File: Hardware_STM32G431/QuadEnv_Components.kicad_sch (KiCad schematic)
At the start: 54 parts, among them J1 Conn_01x04_Male, J2 Conn_01x04_Male, J3 Conn_01x04_Male, J4 Conn_01x04_Male, J5 SWD_Header, J6 Eurorack_10_pin_power, J7 USB_B_Micro, U1 STM32G431C6T6, U2 LD1117-3.3-4Tab, U3 CD40109B, U4 TL074

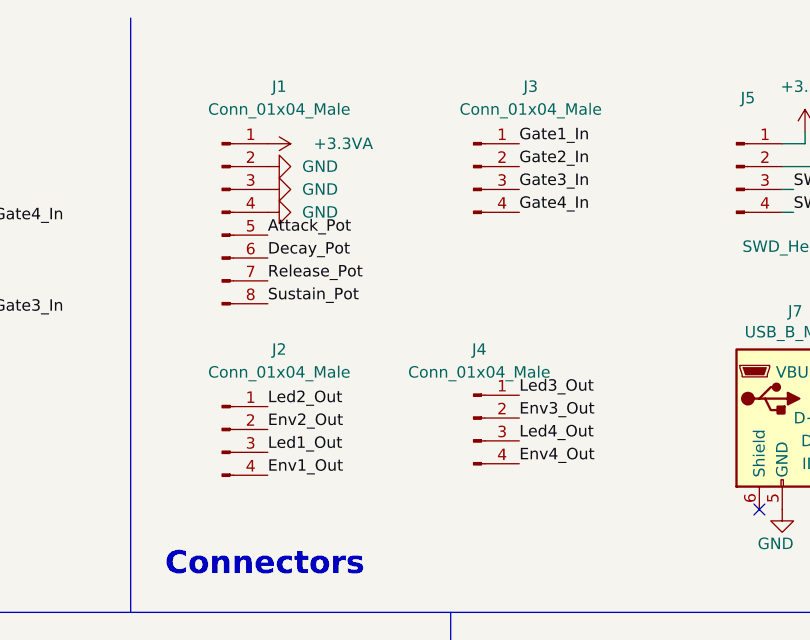
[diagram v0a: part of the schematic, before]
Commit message: First draft of control PCB complete
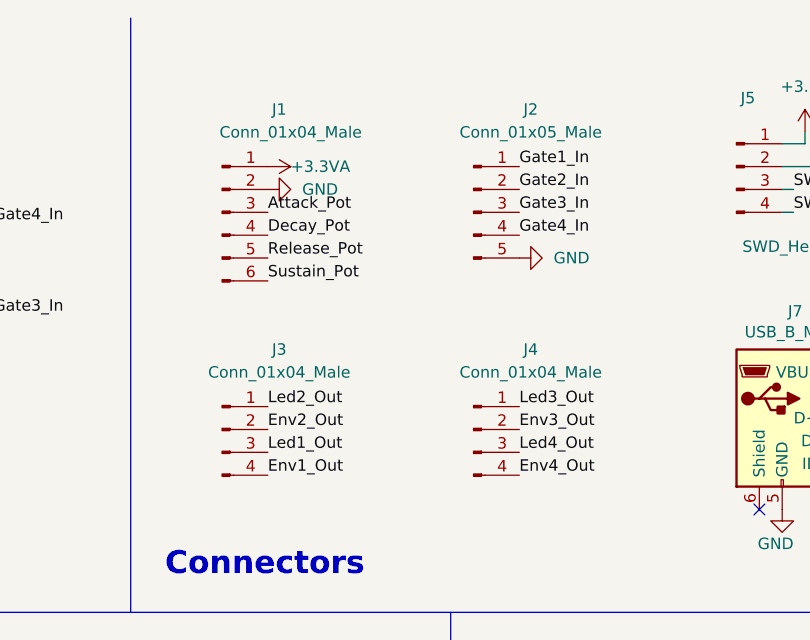
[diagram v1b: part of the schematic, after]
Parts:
- J1: footprint Connector_PinHeader_2.54mm:PinHeader_1x08_P2.54mm_Vertical -> Connector_PinSocket_2.54mm:PinSocket_1x06_P2.54mm_Vertical; symbol Connector:Conn_01x08_Male -> Connector:Conn_01x06_Male
- J2: renamed from J3; value Conn_01x04_Male -> Conn_01x05_Male; footprint Connector_PinHeader_2.54mm:PinHeader_1x04_P2.54mm_Vertical -> Connector_PinSocket_2.54mm:PinSocket_1x05_P2.54mm_Vertical; symbol Connector:Conn_01x04_Male -> Connector:Conn_01x05_Male
- J3: renamed from J2; footprint Connector_PinHeader_2.54mm:PinHeader_1x04_P2.54mm_Vertical -> Connector_PinSocket_2.54mm:PinSocket_1x04_P2.54mm_Vertical
- J4: footprint Connector_PinHeader_2.54mm:PinHeader_1x04_P2.54mm_Vertical -> Connector_PinSocket_2.54mm:PinSocket_1x04_P2.54mm_Vertical
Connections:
- net Attack_Pot: now also J1.3 (Pin_3); no longer J1.5 (Pin_5)
- net Decay_Pot: now also J1.4 (Pin_4); no longer J1.6 (Pin_6)
- net GND: now also J2.5 (Pin_5); no longer J1.3 (Pin_3), J1.4 (Pin_4)
- net Release_Pot: now also J1.5 (Pin_5); no longer J1.7 (Pin_7)
- net Sustain_Pot: now also J1.6 (Pin_6); no longer J1.8 (Pin_8)
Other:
- moved on the sheet: J4

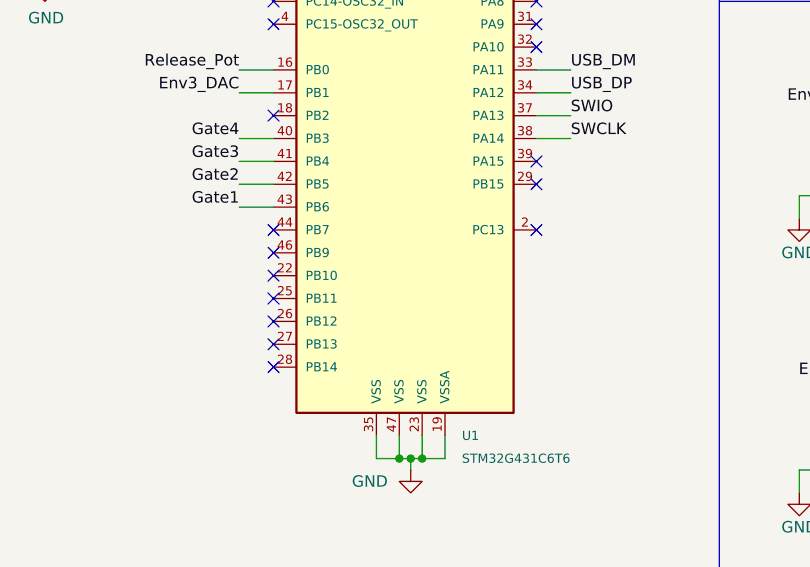
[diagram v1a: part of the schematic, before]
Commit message: Added PWM Test code
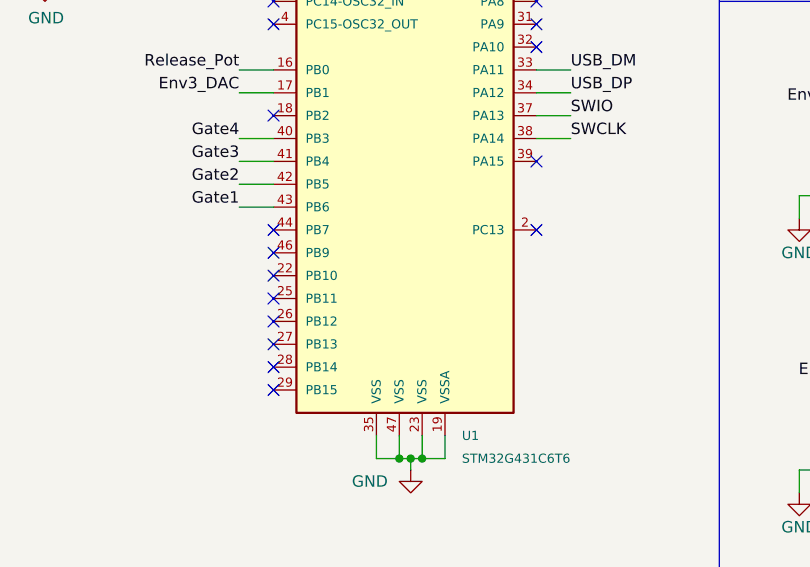
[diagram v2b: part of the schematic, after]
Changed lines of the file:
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@@
   (no_connect (at 45.72 78.74))
   (no_connect (at 261.62 67.31))
-  (no_connect (at 74.93 99.06))
+  (no_connect (at 45.72 121.92))
   (wire (pts (xy 198.12 118.11) (xy 198.12 123.19))
     (stroke (width 0) (type solid) (color 0 0 0 0))

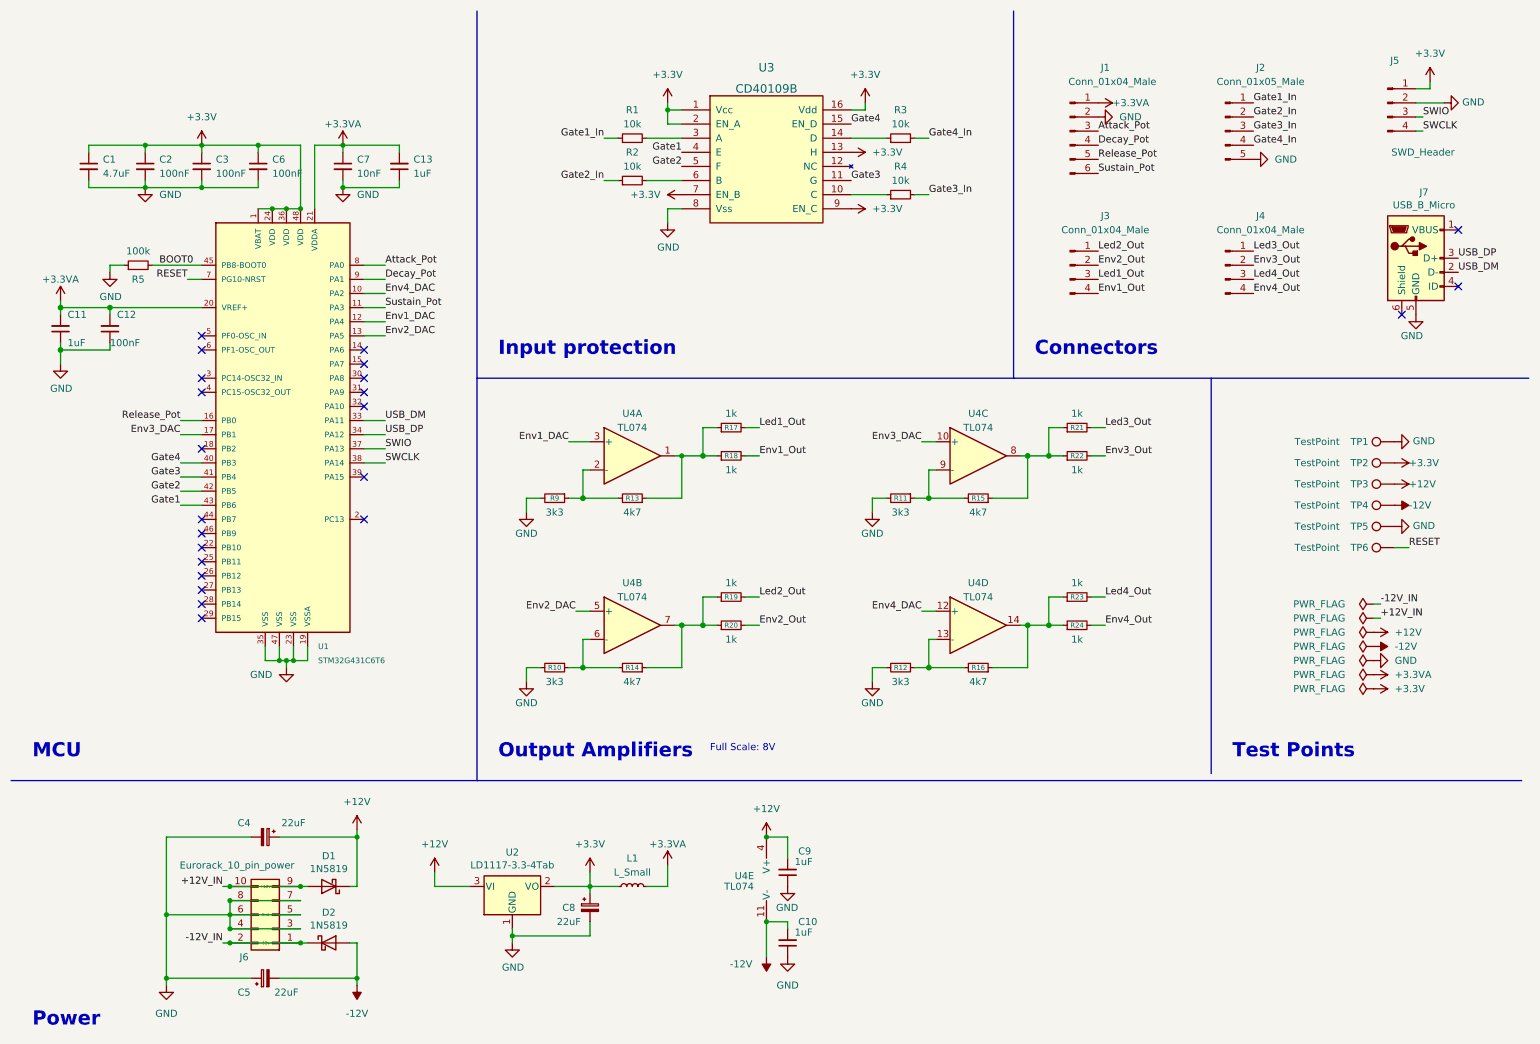
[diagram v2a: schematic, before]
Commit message: Clean up project for manufacture
Fixed LED ordering bug on control board
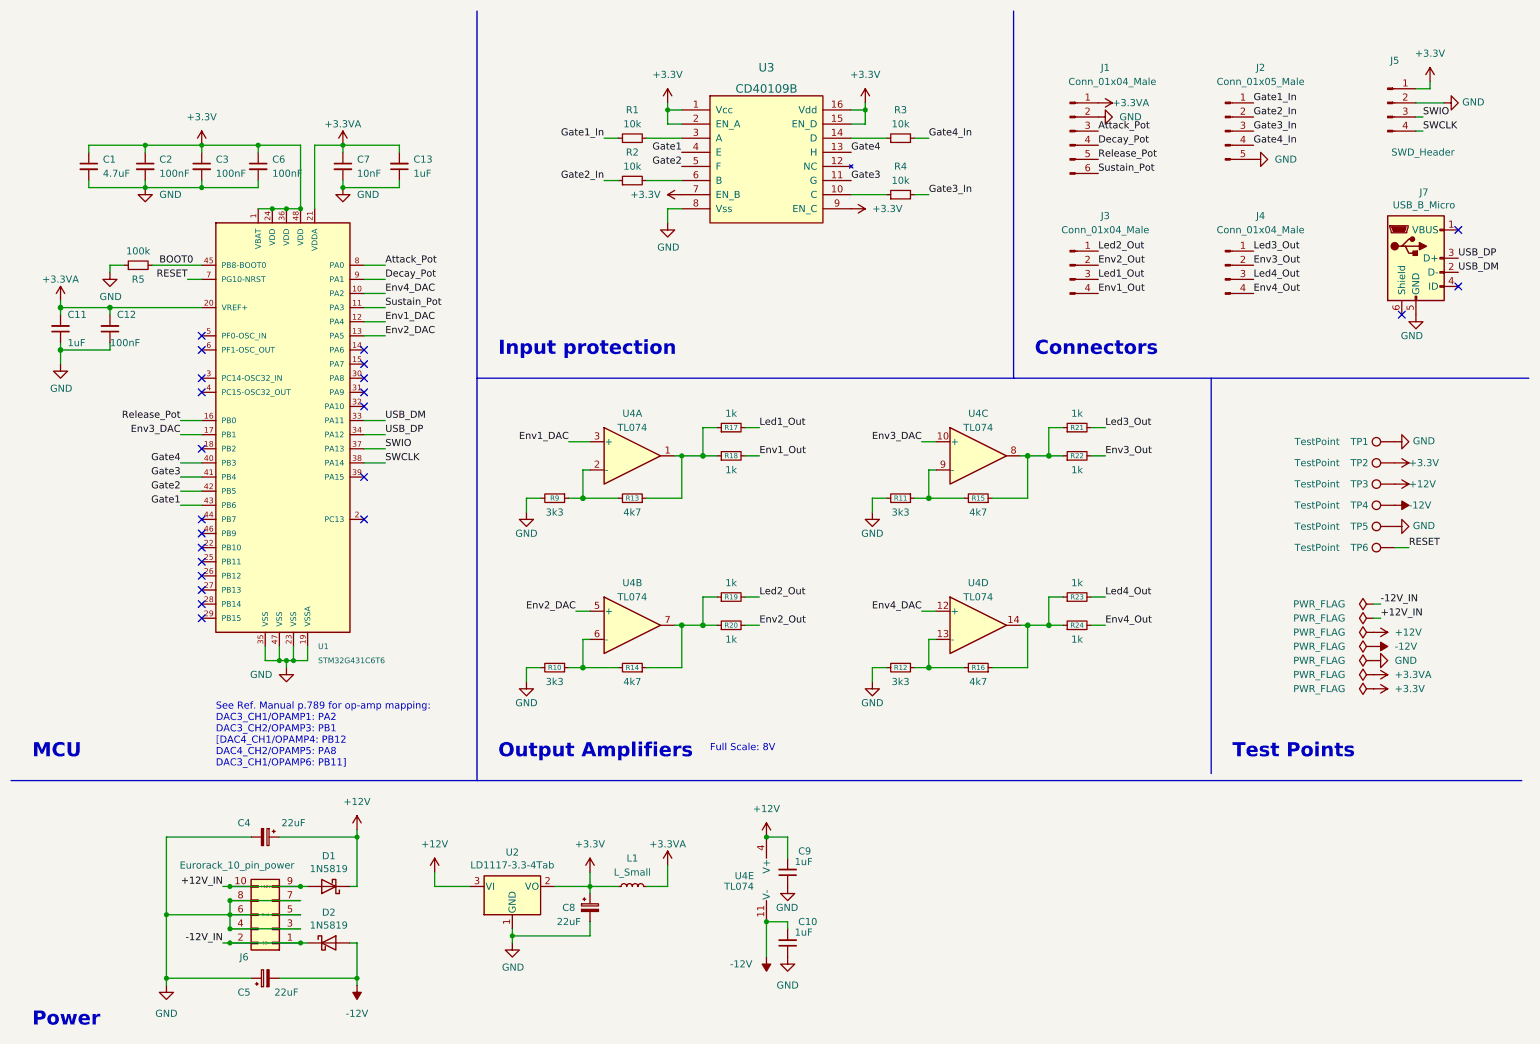
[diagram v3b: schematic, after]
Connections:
- net +3.3V: now also U3.15 (EN_D); no longer U3.13 (H)
- net Gate4: now also U3.13 (H); no longer U3.15 (EN_D)
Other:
- note added: "See Ref. Manual p.789 for op-amp mapping: DAC3_CH1/OPAMP1: PA2 DAC3_CH2/OPAMP3: PB1 [DAC4_CH1/OPAMP4: PB12 DAC4_CH2/OPAMP5: PA8 DAC3_CH1/OPAMP6: PB11]"
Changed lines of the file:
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@@
   (junction (at 73.66 186.69) (diameter 0) (color 0 0 0 0)
+  )
+  (junction (at 165.1 30.48) (diameter 0) (color 0 0 0 0)
   )
   (junction (at 147.32 176.53) (diameter 0) (color 0 0 0 0)
@@
     (stroke (width 0) (type default) (color 0 0 0 0))
   )
+  (wire (pts (xy 162.56 33.02) (xy 165.1 33.02))
+    (stroke (width 0) (type default) (color 0 0 0 0))
+  )
   (wire (pts (xy 101.6 177.8) (xy 101.6 179.07))
     (stroke (width 0) (type default) (color 0 0 0 0))
@@
     (stroke (width 0) (type default) (color 0 0 0 0))
   )
+  (wire (pts (xy 165.1 33.02) (xy 165.1 30.48))
+    (stroke (width 0) (type default) (color 0 0 0 0))
+  )
   (wire (pts (xy 151.13 176.53) (xy 151.13 177.8))
     (stroke (width 0) (type default) (color 0 0 0 0))
@@
   (wire (pts (xy 115.57 167.64) (xy 115.57 170.18))
     (stroke (width 0) (type default) (color 0 0 0 0))
+  )
+  (text "See Ref. Manual p.789 for op-amp mapping:\nDAC3_CH1/OPAMP1: PA2\nDAC3_CH2/OPAMP3: PB1\n[DAC4_CH1/OPAMP4: PB12\nDAC4_CH2/OPAMP5: PA8\nDAC3_CH1/OPAMP6: PB11]\n\n\n\n"
+    (at 48.26 154.94 0)
+    (effects (font (size 1.27 1.27)) (justify left bottom))
   )
   (text "Full Scale: 8V" (at 137.16 146.05 0)
@@
     (effects (font (size 1.27 1.27)) (justify left bottom))
   )
-  (label "Gate4" (at 162.56 33.02 0)
+  (label "Gate4" (at 162.56 38.1 0)
     (effects (font (size 1.27 1.27)) (justify left bottom))
   )
@@
     (pin "2")
   )
-  (symbol (lib_name "+3.3V_1") (lib_id "power:+3.3V") (at 162.56 38.1 270) (unit 1)
-    (in_bom yes) (on_board yes) (fields_autoplaced)
-    (property "Reference" "#PWR0108" (id 0) (at 158.75 38.1 0)
-      (effects (font (size 1.27 1.27)) hide)
-    )
-    (property "Value" "+3.3V" (id 1) (at 166.37 38.0999 90)
-      (effects (font (size 1.27 1.27)) (justify left))
-    )
-    (property "Footprint" "" (id 2) (at 162.56 38.1 0)
-      (effects (font (size 1.27 1.27)) hide)
-    )
-    (property "Datasheet" "" (id 3) (at 162.56 38.1 0)
-      (effects (font (size 1.27 1.27)) hide)
-    )
-    (pin "1")
-  )
   (symbol (lib_id "Connector:Conn_01x05_Male") (at 229.87 34.29 0) (unit 1)
     (in_bom yes) (on_board yes)
@@
       (reference "#PWR0107") (unit 1) (value "+3.3V") (footprint "")
     )
-    (path "/fa107435-2d32-4d94-833b-80d0f9a40a44"
-      (reference "#PWR0108") (unit 1) (value "+3.3V") (footprint "")
-    )
     (path "/4c7f8d14-f24c-4d20-8d5f-ec91fa3398fd"

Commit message: Corrections to schematic to fix sustain and release pots being switched
+Updated project to use production module parts and connections
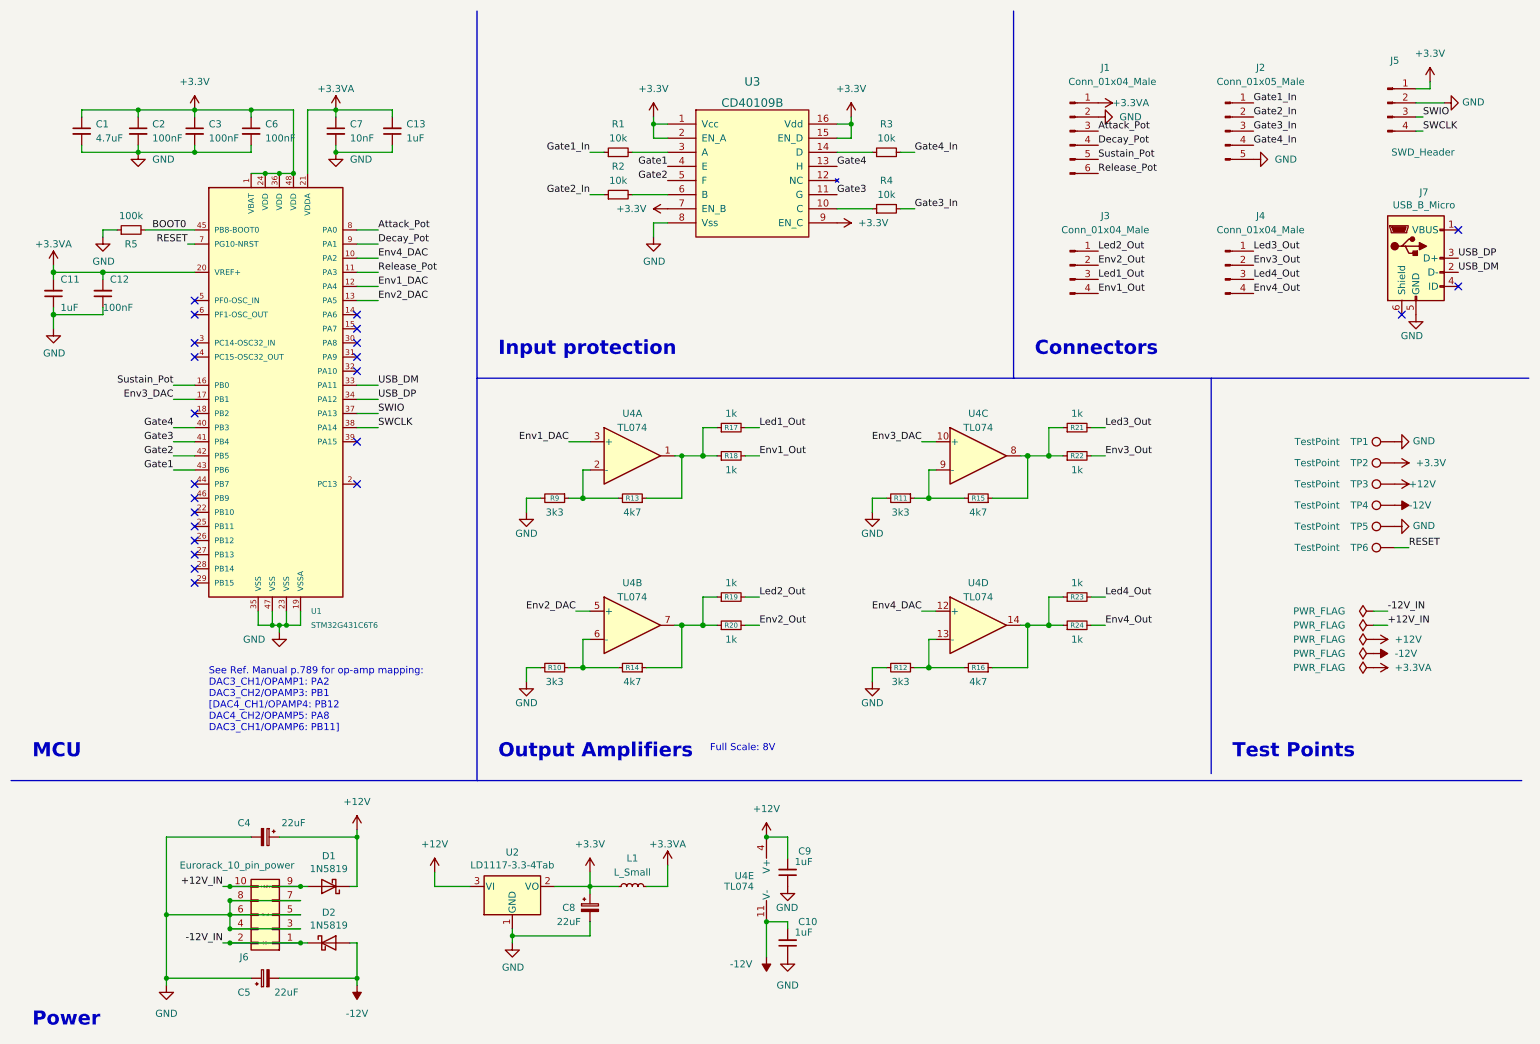
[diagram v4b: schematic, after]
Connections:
- net +3V3 is gone; now on net +3.3V: TP2.1
- net Release_Pot: now also J1.6 (Pin_6), U1.11 (PA3); no longer J1.5 (Pin_5), U1.16 (PB0)
- net Sustain_Pot: now also J1.5 (Pin_5), U1.16 (PB0); no longer J1.6 (Pin_6), U1.11 (PA3)
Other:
- moved on the sheet: C1, C11, C12, C13, C2, C3, C6, C7, R1, R2, R3, R4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
